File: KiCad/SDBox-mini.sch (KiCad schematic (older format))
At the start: 25 parts, among them J1 DB25_Male, J2 Conn_02x03_Odd_Even, J3 Micro_SD_Card, J4 USB_B_Micro, U1 ATmega328P-AU, U2 LM1117-3.3, U3 74LVC3G17, U4 74HCT2G17, Y1 Crystal_GND24_Small

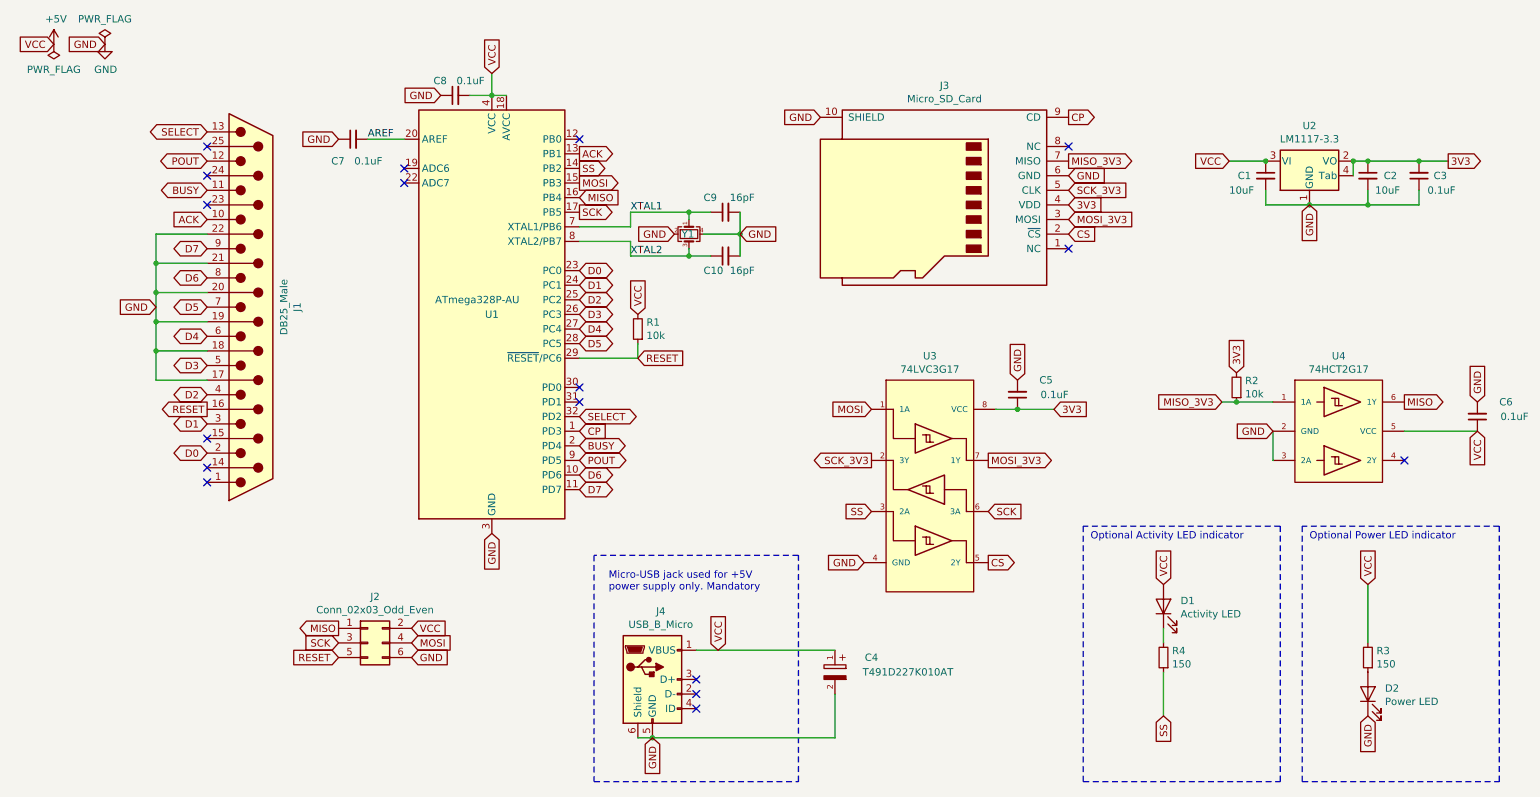
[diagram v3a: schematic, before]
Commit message: added decoupling cap near ICSP-header VCC and relabeled ordering of components
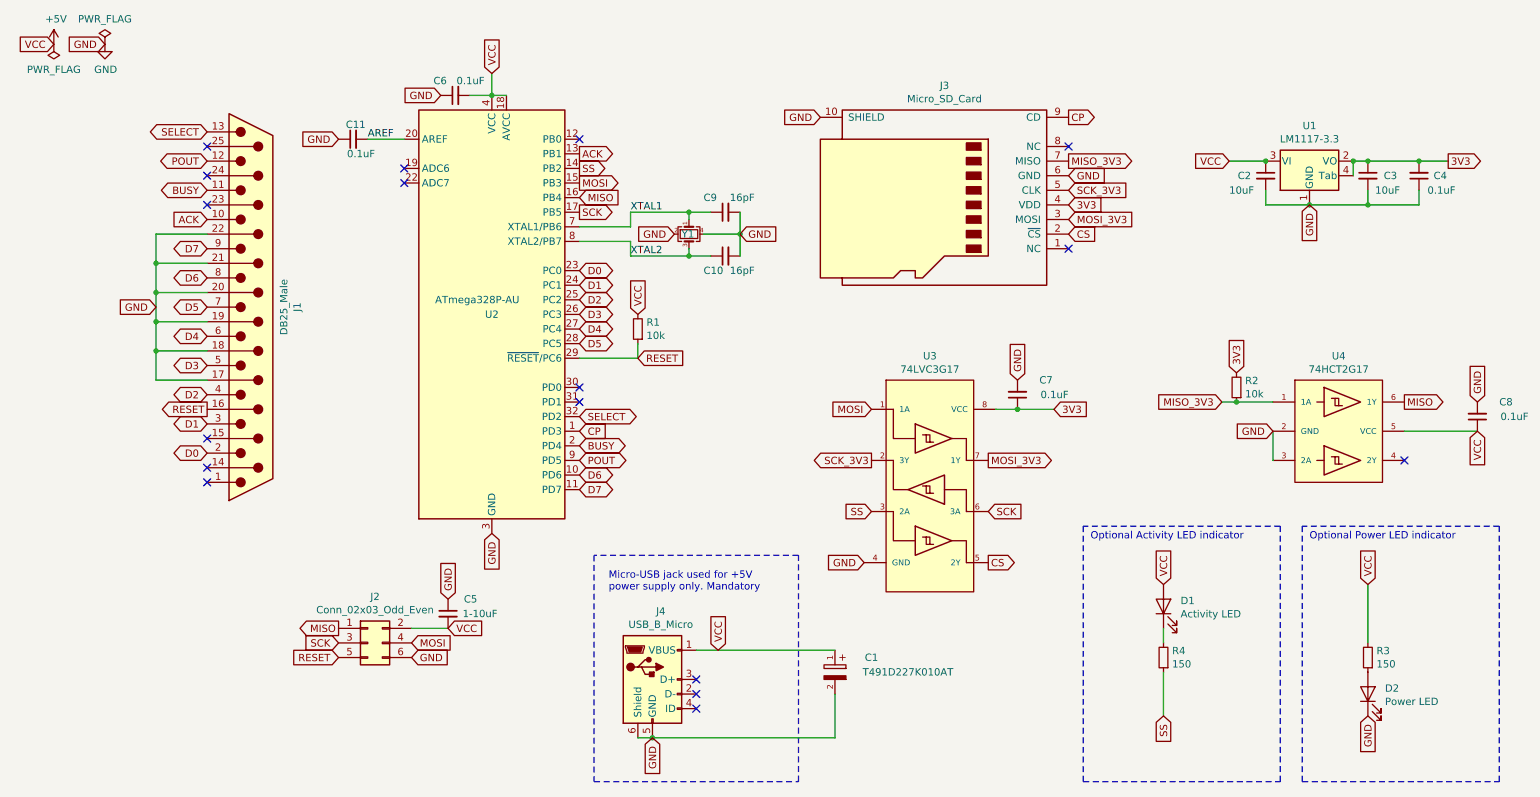
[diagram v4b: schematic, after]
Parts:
- added C5: 1-10uF, Capacitor_SMD:C_0805_2012Metric_Pad1.15x1.40mm_HandSolder, symbol Device:C_Small
- renumbered C4 to C1, C7 to C11, C1 to C2, C2 to C3, C3 to C4, C8 to C6, C5 to C7, C6 to C8, U2 to U1, U1 to U2
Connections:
- net +5V: now also C5.2
- net GND: now also C5.1
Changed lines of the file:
@@
 $EndDescr
 $Comp
-L Device:C_Small C7
+L Device:C_Small C11
 U 1 1 606A3110
 P 3000 1600
-F 0 "C7" V 2850 1750 50  0000 R CNN
-F 1 "0.1uF" V 2850 1400 50  0000 L CNN
+F 0 "C11" V 3100 1650 50  0000 R CNN
+F 1 "0.1uF" V 2900 1450 50  0000 L CNN
 F 2 "Capacitor_SMD:C_0603_1608Metric_Pad1.05x0.95mm_HandSolder" H 3000 1600 50  0001 C CNN
 F 3 "~" H 3000 1600 50  0001 C CNN
@@
 D0
 $Comp
-L MCU_Microchip_ATmega:ATmega328P-AU U1
+L MCU_Microchip_ATmega:ATmega328P-AU U2
 U 1 1 60F7C9EE
 P 3950 2800
-F 0 "U1" H 3950 2800 50  0000 C CNN
+F 0 "U2" H 3950 2800 50  0000 C CNN
 F 1 "ATmega328P-AU" H 3850 2900 50  0000 C CNN
 F 2 "Package_QFP:TQFP-32_7x7mm_P0.8mm" H 3950 2800 50  0001 C CIN
@@
 Connection ~ 5650 2250
 $Comp
-L Device:C_Small C8
+L Device:C_Small C6
 U 1 1 60FA7C64
 P 3700 1300
-F 0 "C8" V 3800 1450 50  0000 R CNN
+F 0 "C6" V 3800 1450 50  0000 R CNN
 F 1 "0.1uF" V 3800 1100 50  0000 L CNN
 F 2 "Capacitor_SMD:C_0603_1608Metric_Pad1.05x0.95mm_HandSolder" H 3700 1300 50  0001 C CNN
@@
 SCK_3V3
 $Comp
-L Regulator_Linear:LM1117-3.3 U2
+L Regulator_Linear:LM1117-3.3 U1
 U 1 1 61034FEA
 P 9550 1750
-F 0 "U2" H 9550 1992 50  0000 C CNN
+F 0 "U1" H 9550 1992 50  0000 C CNN
 F 1 "LM1117-3.3" H 9550 1901 50  0000 C CNN
 F 2 "Package_TO_SOT_SMD:SOT-223" H 9550 1750 50  0001 C CNN
@@
 VCC
 $Comp
-L Device:C_Small C1
+L Device:C_Small C2
 U 1 1 610421CE
 P 9250 1850
-F 0 "C1" H 9150 1850 50  0000 R CNN
+F 0 "C2" H 9150 1850 50  0000 R CNN
 F 1 "10uF" H 9000 1750 50  0000 L CNN
 F 2 "Capacitor_SMD:C_1206_3216Metric_Pad1.42x1.75mm_HandSolder" H 9250 1850 50  0001 C CNN
@@
 $EndComp
 $Comp
-L Device:C_Small C2
+L Device:C_Small C3
 U 1 1 610444D0
 P 9950 1850
-F 0 "C2" H 10150 1850 50  0000 R CNN
+F 0 "C3" H 10150 1850 50  0000 R CNN
 F 1 "10uF" H 10000 1750 50  0000 L CNN
 F 2 "Capacitor_SMD:C_1206_3216Metric_Pad1.42x1.75mm_HandSolder" H 9950 1850 50  0001 C CNN
@@
 $EndComp
 $Comp
-L Device:C_Small C3
+L Device:C_Small C4
 U 1 1 6104580B
 P 10300 1850
-F 0 "C3" H 10200 1850 50  0000 R CNN
+F 0 "C4" H 10200 1850 50  0000 R CNN
 F 1 "0.1uF" H 10050 1950 50  0000 L CNN
 F 2 "Capacitor_SMD:C_0603_1608Metric_Pad1.05x0.95mm_HandSolder" H 10300 1850 50  0001 C CNN
@@
 Text GLabel 10500 1750 2    50   Output ~ 0
 3V3
-Text GLabel 3400 4950 2    50   Input ~ 0
+Text GLabel 3650 4950 2    50   Input ~ 0
 VCC
 Text GLabel 3400 5150 2    50   Input ~ 0
 GND
 $Comp
-L Device:C_Small C5
+L Device:C_Small C7
 U 1 1 61017825
 P 7550 3350
-F 0 "C5" H 7400 3250 50  0000 R CNN
+F 0 "C7" H 7400 3250 50  0000 R CNN
 F 1 "0.1uF" H 7200 3350 50  0000 L CNN
 F 2 "Capacitor_SMD:C_0603_1608Metric_Pad1.05x0.95mm_HandSolder" H 7550 3350 50  0001 C CNN
@@
 $EndComp
 $Comp
-L Device:C_Small C6
+L Device:C_Small C8
 U 1 1 61087309
 P 10700 3500
-F 0 "C6" H 10550 3400 50  0000 R CNN
+F 0 "C8" H 10550 3400 50  0000 R CNN
 F 1 "0.1uF" H 10350 3500 50  0000 L CNN
 F 2 "Capacitor_SMD:C_0603_1608Metric_Pad1.05x0.95mm_HandSolder" H 10700 3500 50  0001 C CNN
@@
 	6050 6000 6050 4450
 $Comp
-L SDBox-mini:T491D227K010AT C4
+L SDBox-mini:T491D227K010AT C1
 U 1 1 60F9E387
 P 6300 5300
-F 0 "C4" V 6450 5050 50  0000 C CNN
+F 0 "C1" V 6450 5050 50  0000 C CNN
 F 1 "T491D227K010AT" V 6350 4800 50  0000 C CNN
 F 2 "SDBox-mini:CAPMP7343X430N" H 6300 5300 50  0001 L BNN
@@
 Wire Wire Line
 	8550 5250 8550 5550
+$Comp
+L Device:C_Small C5
+U 1 1 61173877
+P 3650 4850
+F 0 "C5" H 3850 4950 50  0000 R CNN
+F 1 "1-10uF" H 3750 4850 50  0000 L CNN
+F 2 "Capacitor_SMD:C_0805_2012Metric_Pad1.15x1.40mm_HandSolder" H 3650 4850 50  0001 C CNN
+F 3 "~" H 3650 4850 50  0001 C CNN
+	1    3650 4850
+	1    0    0    -1
+$EndComp
+Wire Wire Line
+	3650 4950 3400 4950
+Text GLabel 3650 4750 1    50   Input ~ 0
+GND
 $EndSCHEMATC

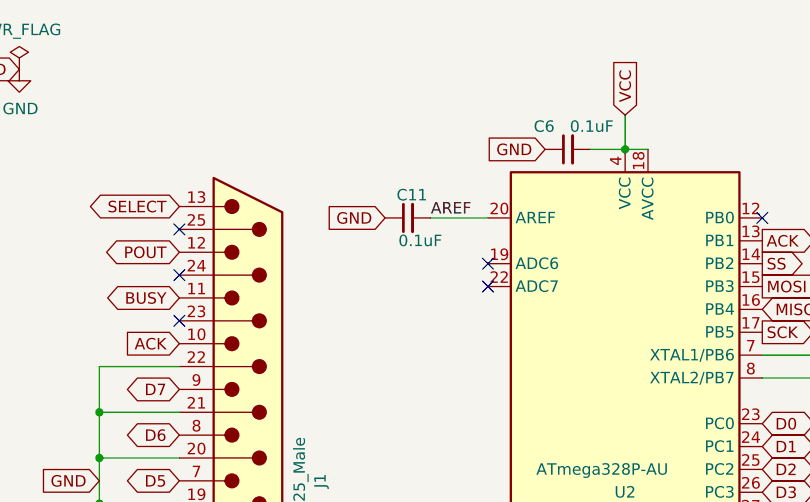
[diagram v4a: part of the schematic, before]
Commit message: removed AREF capacitor, it was unnecessary
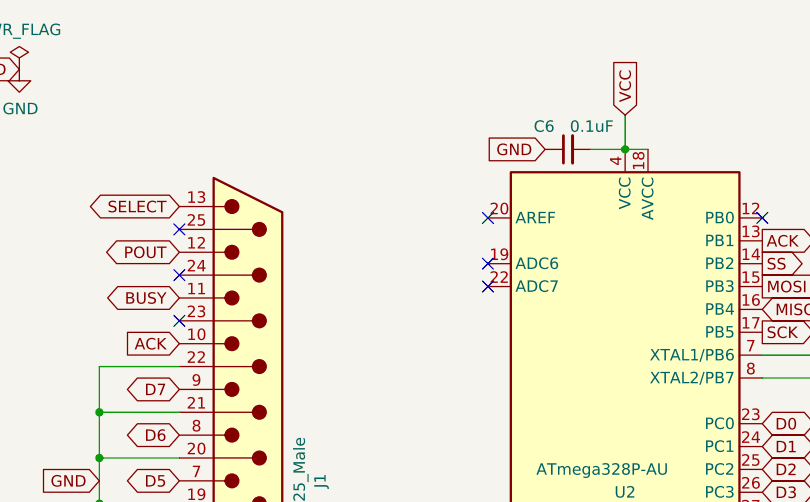
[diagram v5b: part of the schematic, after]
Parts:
- removed C11: 0.1uF, Capacitor_SMD:C_0603_1608Metric_Pad1.05x0.95mm_HandSolder, symbol Device:C_Small
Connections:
- net AREF: no longer names the net of U2.20 (AREF)
- no-connect marks 17 -> 18
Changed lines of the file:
@@
 Comment4 ""
 $EndDescr
-$Comp
-L Device:C_Small C11
-U 1 1 606A3110
-P 3000 1600
-F 0 "C11" V 3100 1650 50  0000 R CNN
-F 1 "0.1uF" V 2900 1450 50  0000 L CNN
-F 2 "Capacitor_SMD:C_0603_1608Metric_Pad1.05x0.95mm_HandSolder" H 3000 1600 50  0001 C CNN
-F 3 "~" H 3000 1600 50  0001 C CNN
-	1    3000 1600
-	0    -1   -1   0
-$EndComp
-Text GLabel 2900 1600 0    50   Input ~ 0
-GND
 Text GLabel 950  950  0    50   Input ~ 0
 VCC
@@
 Text GLabel 4950 2800 1    50   Input ~ 0
 VCC
-Text Label 3100 1600 0    50   ~ 0
-AREF
-Wire Wire Line
-	3100 1600 3350 1600
 Wire Wire Line
 	4550 3100 4950 3100
@@
 Text GLabel 3650 4750 1    50   Input ~ 0
 GND
+NoConn ~ 3350 1600
 $EndSCHEMATC

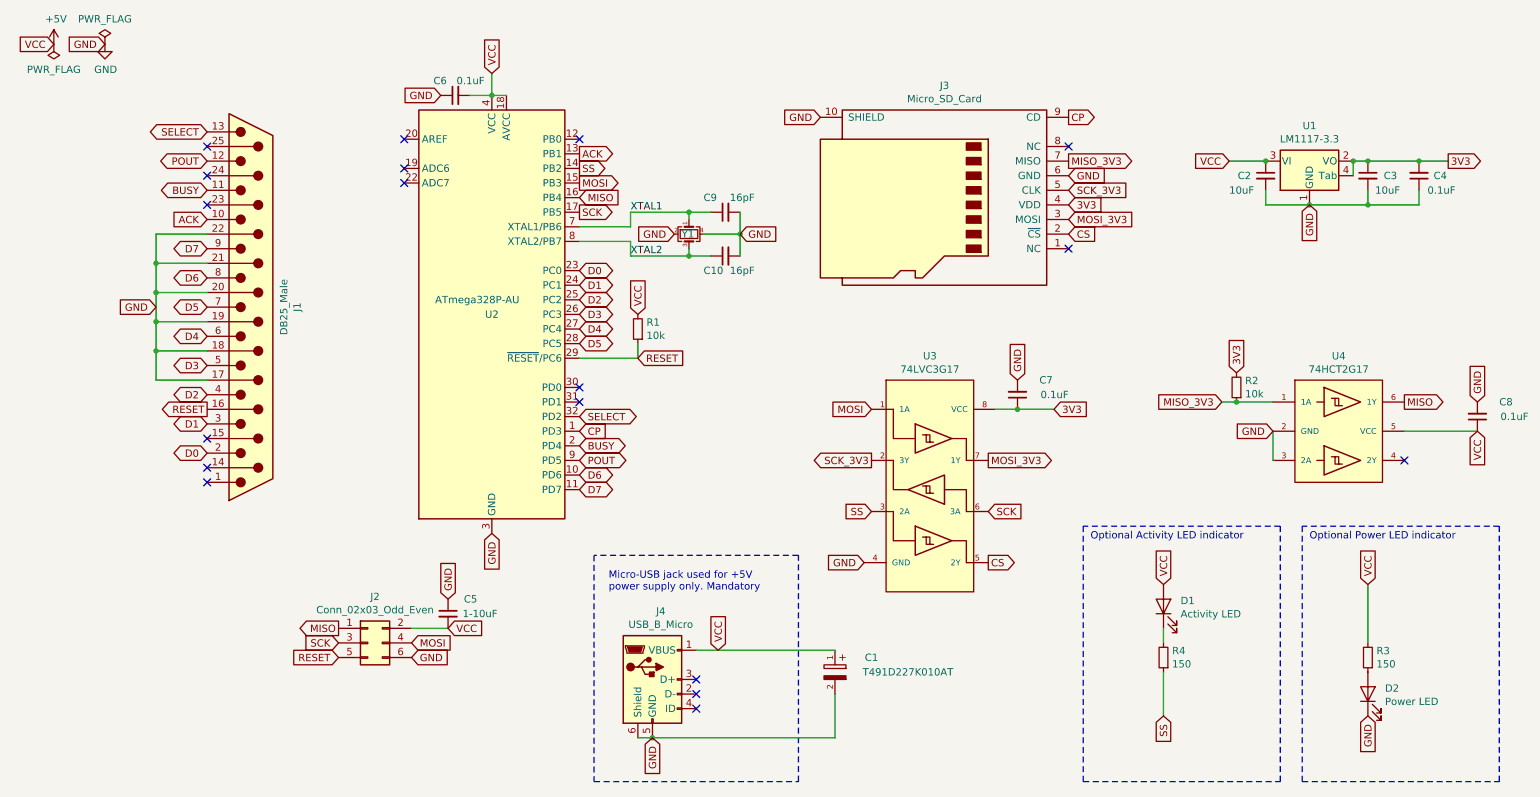
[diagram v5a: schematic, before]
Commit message: changed Activity-LED to be controlled by PB0, added 10k pull-up resistor on SS-line
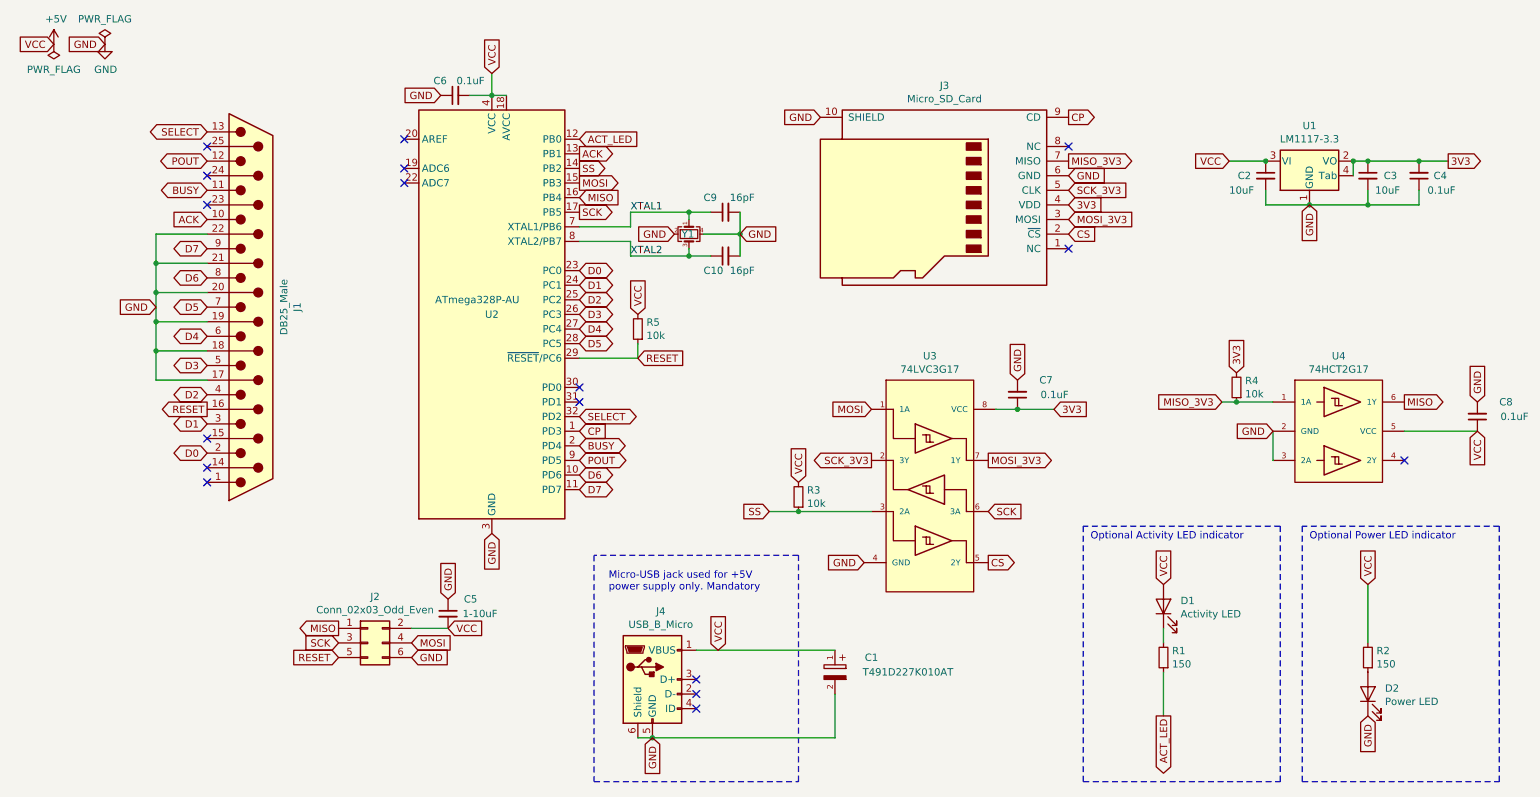
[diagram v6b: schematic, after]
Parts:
- added R3: 10k, Resistor_SMD:R_0603_1608Metric_Pad1.05x0.95mm_HandSolder, symbol Device:R_Small
- renumbered R4 to R1, R3 to R2, R2 to R4, R1 to R5
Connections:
- net +5V: now also R3.2
- net SS: now also R3.1; no longer R1.1
- net ACT_LED: now reaches U2.12 (PB0)
- net ACT_LED: now also R1.1
- no-connect marks 18 -> 17
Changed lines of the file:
@@
 	3950 1300 4050 1300
 $Comp
-L Device:R_Small R1
+L Device:R_Small R5
 U 1 1 60F84B00
 P 4950 2900
-F 0 "R1" H 4891 2854 50  0000 R CNN
+F 0 "R5" H 4891 2854 50  0000 R CNN
 F 1 "10k" H 4891 2945 50  0000 R CNN
 F 2 "Resistor_SMD:R_0603_1608Metric_Pad1.05x0.95mm_HandSolder" H 4950 2900 50  0001 C CNN
@@
 Text GLabel 4950 3100 2    50   Input ~ 0
 RESET
-NoConn ~ 4550 1600
 NoConn ~ 7900 2350
 Text GLabel 10200 3400 2    50   Output ~ 0
@@
 GND
 $Comp
-L Device:R_Small R2
+L Device:R_Small R4
 U 1 1 6101E2BD
 P 9050 3300
-F 0 "R2" H 8991 3254 50  0000 R CNN
+F 0 "R4" H 8991 3254 50  0000 R CNN
 F 1 "10k" H 8991 3345 50  0000 R CNN
 F 2 "Resistor_SMD:R_0603_1608Metric_Pad1.05x0.95mm_HandSolder" H 9050 3300 50  0001 C CNN
@@
 Text GLabel 4550 1800 2    50   Output ~ 0
 SS
-Text GLabel 6550 4150 0    50   Input ~ 0
+Text GLabel 5850 4150 0    50   Input ~ 0
 SS
 $Comp
@@
 $EndComp
 $Comp
-L Device:R_Small R3
+L Device:R_Small R2
 U 1 1 60F8AA52
 P 9950 5150
-F 0 "R3" H 9891 5104 50  0000 R CNN
+F 0 "R2" H 9891 5104 50  0000 R CNN
 F 1 "150" H 9891 5195 50  0000 R CNN
 F 2 "Resistor_SMD:R_0603_1608Metric_Pad1.05x0.95mm_HandSolder" H 9950 5150 50  0001 C CNN
@@
 Text GLabel 8550 4650 1    50   Input ~ 0
 VCC
-Text GLabel 8550 5550 3    50   Input ~ 0
-SS
 $Comp
 L Device:LED D1
@@
 $EndComp
 $Comp
-L Device:R_Small R4
+L Device:R_Small R1
 U 1 1 60FB8FAC
 P 8550 5150
-F 0 "R4" H 8491 5104 50  0000 R CNN
+F 0 "R1" H 8491 5104 50  0000 R CNN
 F 1 "150" H 8491 5195 50  0000 R CNN
 F 2 "Resistor_SMD:R_0603_1608Metric_Pad1.05x0.95mm_HandSolder" H 8550 5150 50  0001 C CNN
@@
 GND
 NoConn ~ 3350 1600
+Text GLabel 4550 1600 2    50   Input ~ 0
+ACT_LED
+Text GLabel 8550 5550 3    50   Output ~ 0
+ACT_LED
+$Comp
+L Device:R_Small R3
+U 1 1 6119A937
+P 6050 4050
+F 0 "R3" H 5991 4004 50  0000 R CNN
+F 1 "10k" H 5991 4095 50  0000 R CNN
+F 2 "Resistor_SMD:R_0603_1608Metric_Pad1.05x0.95mm_HandSolder" H 6050 4050 50  0001 C CNN
+F 3 "~" H 6050 4050 50  0001 C CNN
+	1    6050 4050
+	-1   0    0    1
+$EndComp
+Text GLabel 6050 3950 1    50   Input ~ 0
+VCC
+Wire Wire Line
+	5850 4150 6050 4150
+Connection ~ 6050 4150
+Wire Wire Line
+	6050 4150 6550 4150
 $EndSCHEMATC
